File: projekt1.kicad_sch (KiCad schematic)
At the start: 94 parts, among them IC1 TPS563300DRLR, J1 V1, J2 V1, K1 1461103-1, K2 SANYOU_SRD_Form_B, Q1 MMBT3904, Q2 MMBT3904, SW1 SW_Push, SW10 SW_Push, SW11 SW_Push, SW12 SW_Push, SW2 SW_Push, SW3 SW_Push, SW4 SW_Push, SW5 SW_Push, SW6 SW_Push, SW7 SW_Push, SW8 SW_Push, SW9 SW_Push, U1 STM32F030C8Tx, U2 ESP-12E, U4 LTV-824, U5 PN5321A3HN_C1xx, Y1 ABM3-8.000MHZ-D2Y

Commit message: filled all footprints
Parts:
- AE1: value Antena -> Antenna; footprint (none) -> RF_Antenna:Coilcraft_MA5532-AE_RFID
- C1, C10, C11, C12, C13, C14, C15, C16, C17, C18, C19, C2, C20, C21, C22, C23, C24, C25, C26, C27, C28, C29, C3, C30, C31, C32, C4, C5, C6, C7, C8, C9: footprint (none) -> Capacitor_SMD:C_0603_1608Metric_Pad1.08x0.95mm_HandSolder
- J1, J2: footprint (none) -> TerminalBlock_TE-Connectivity:TerminalBlock_TE_282834-2_1x02_P2.54mm_Horizontal
- L1: footprint (none) -> Inductor_SMD:L_0603_1608Metric_Pad1.05x0.95mm_HandSolder
- L2, L3: footprint (none) -> Inductor_SMD:L_0201_0603Metric_Pad0.64x0.40mm_HandSolder
- R1, R10, R11, R12, R13, R14, R15, R17, R18, R19, R2, R4, R6, R7, R8, R9: footprint (none) -> Resistor_SMD:R_0603_1608Metric_Pad0.98x0.95mm_HandSolder
- R16: footprint (none) -> Resistor_SMD:R_0603_1608Metric
- R3: value R -> 300; footprint (none) -> Resistor_SMD:R_0603_1608Metric
- R5: value 10kR -> 10K; footprint (none) -> Resistor_SMD:R_0603_1608Metric_Pad0.98x0.95mm_HandSolder
- SW1, SW10, SW11, SW12, SW2, SW3, SW4, SW5, SW6, SW7, SW8, SW9: footprint (none) -> Button_Switch_SMD:SW_DIP_SPSTx01_Slide_Copal_CHS-01A_W5.08mm_P1.27mm_JPin
- Y1: footprint (none) -> Crystal:Crystal_SMD_Abracon_ABM3-2Pin_5.0x3.2mm_HandSoldering
- Y2: renamed from 27.12MHz1; value CX3225GB -> 27.12MHz1; footprint (none) -> Crystal:Crystal_SMD_Abracon_ABM3-2Pin_5.0x3.2mm_HandSoldering; Memory (none) -> CX3225GB

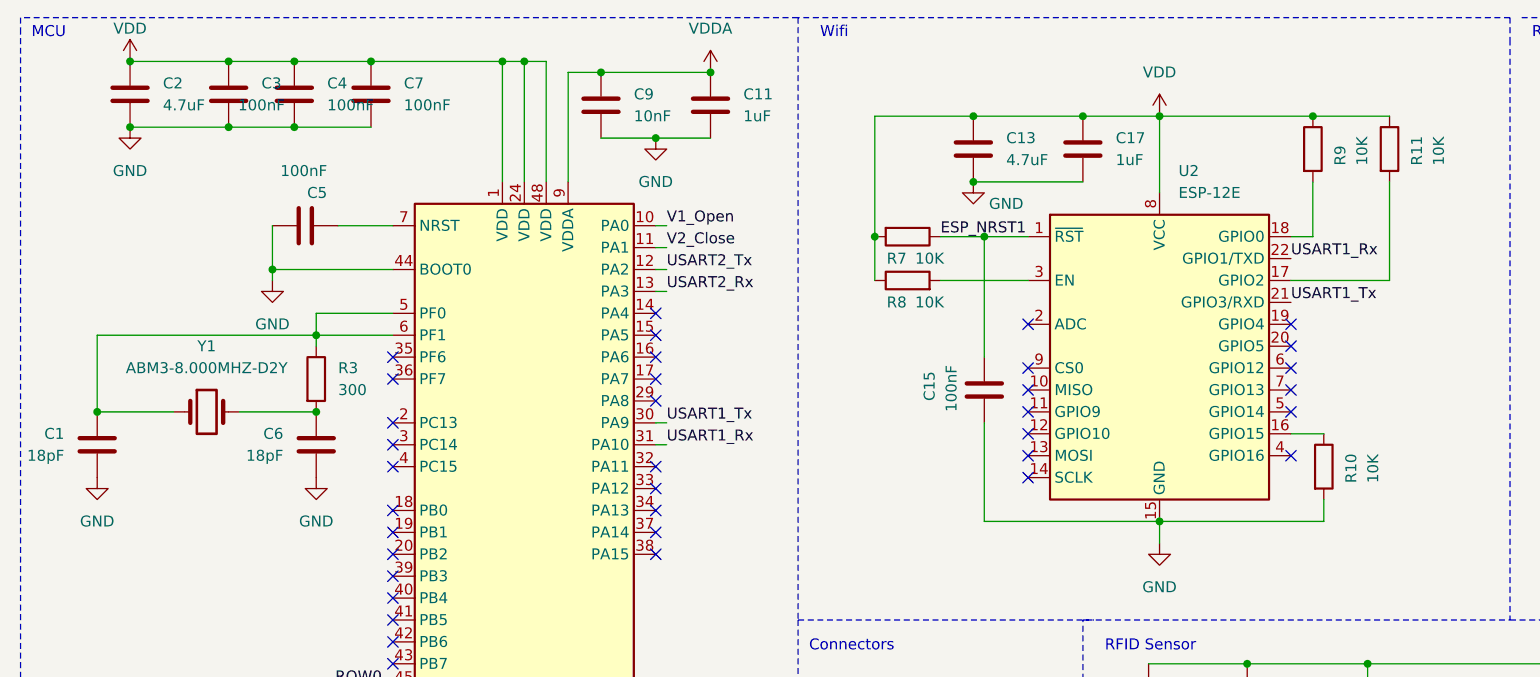
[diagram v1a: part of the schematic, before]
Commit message: initial pcb elements arrangement
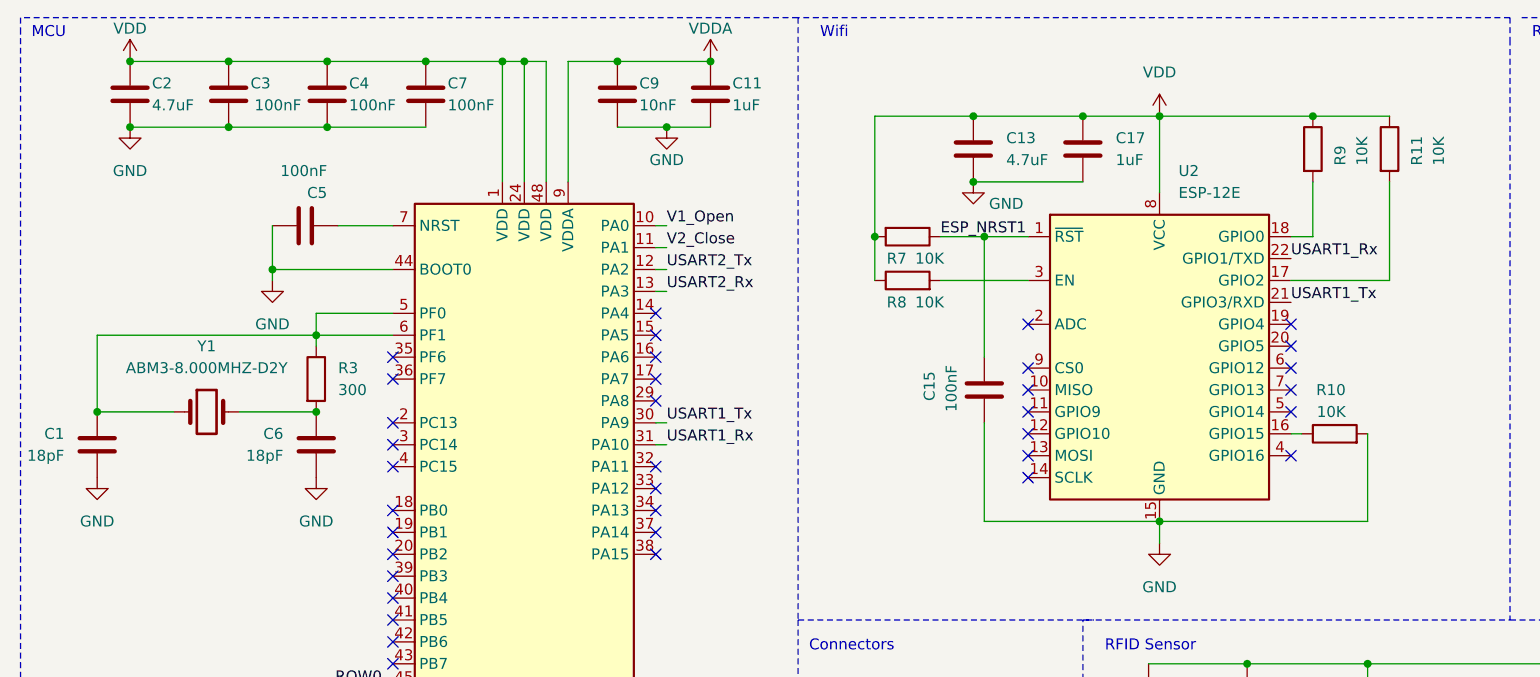
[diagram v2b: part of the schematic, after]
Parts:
- R16: footprint Resistor_SMD:R_0603_1608Metric -> Resistor_SMD:R_0603_1608Metric_Pad0.98x0.95mm_HandSolder
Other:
- moved on the sheet: C11, C4, C7, C9, R10

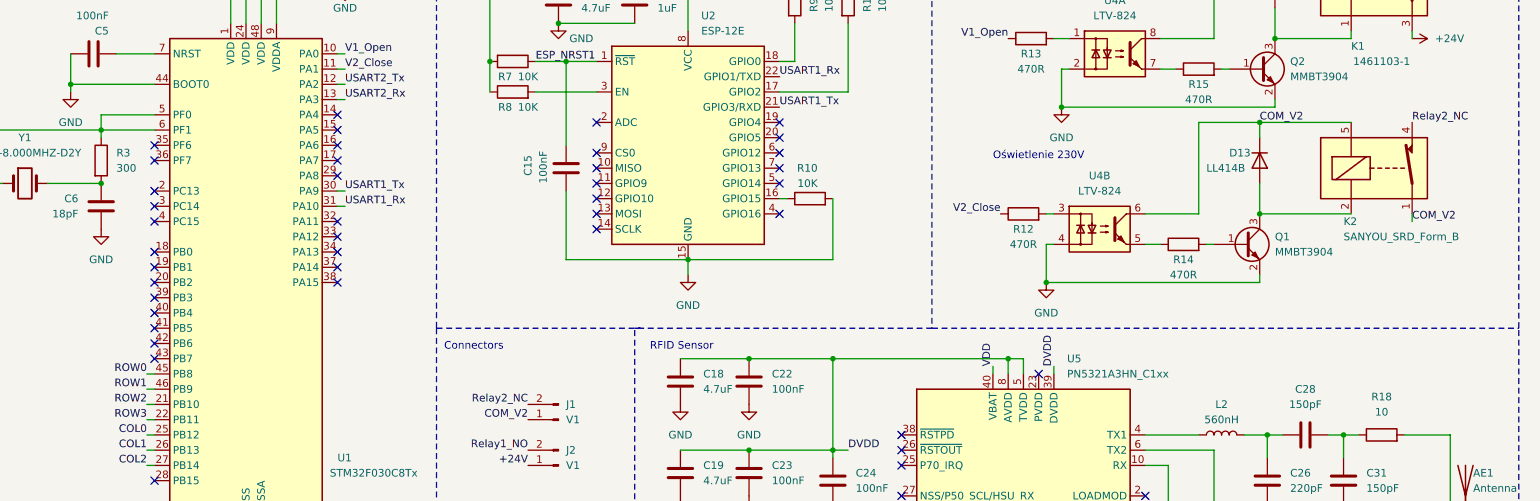
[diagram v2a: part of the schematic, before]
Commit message: pcb connections implemented
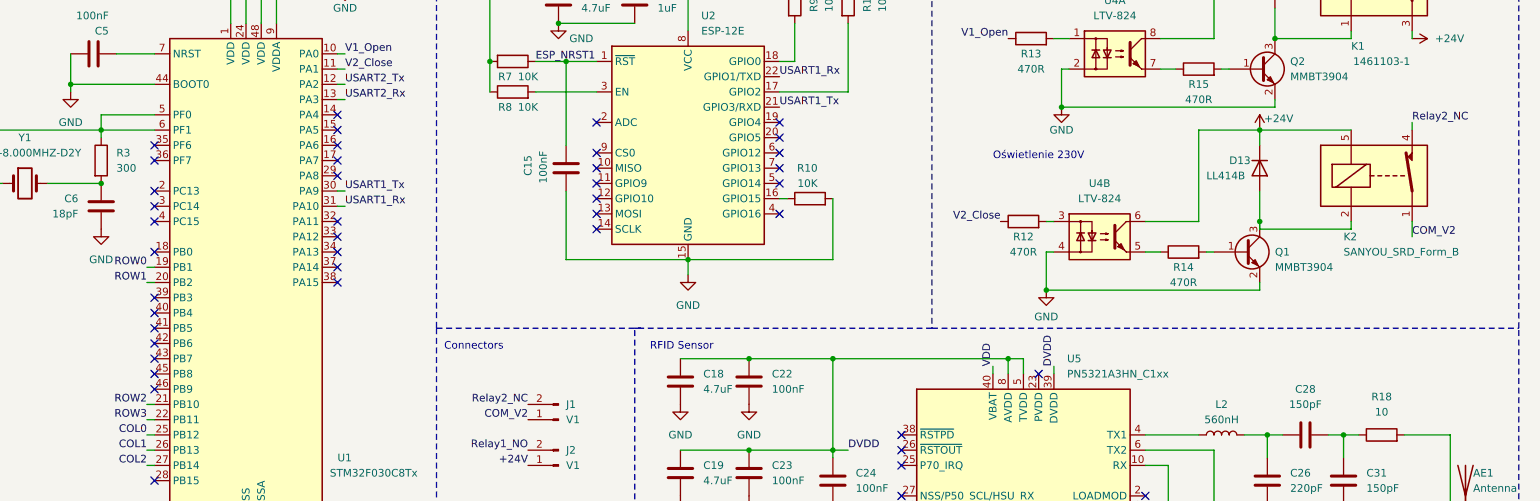
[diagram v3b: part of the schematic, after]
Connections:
- net +24V: now also D13.1 (K), K2.5, U4.6
- net COM_V2: no longer D13.1 (K), K2.5, U4.6
- net ROW0: now also U1.19 (PB1); no longer U1.45 (PB8)
- net ROW1: now also U1.20 (PB2); no longer U1.46 (PB9)
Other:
- moved on the sheet: D13, K2, Q1, R12, R14, U4B

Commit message: changed connector footprint and adjusted paths width
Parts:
- J1: footprint TerminalBlock_TE-Connectivity:TerminalBlock_TE_282834-2_1x02_P2.54mm_Horizontal -> TerminalBlock:TerminalBlock_Altech_AK300-2_P5.00mm
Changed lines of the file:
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@@
       (effects (font (size 1.27 1.27)) (justify right))
     )
-    (property "Footprint" "TerminalBlock_TE-Connectivity:TerminalBlock_TE_282834-2_1x02_P2.54mm_Horizontal" (at 123.19 97.79 0)
+    (property "Footprint" "TerminalBlock:TerminalBlock_Altech_AK300-2_P5.00mm" (at 123.19 97.79 0)
       (effects (font (size 1.27 1.27)) hide)
     )

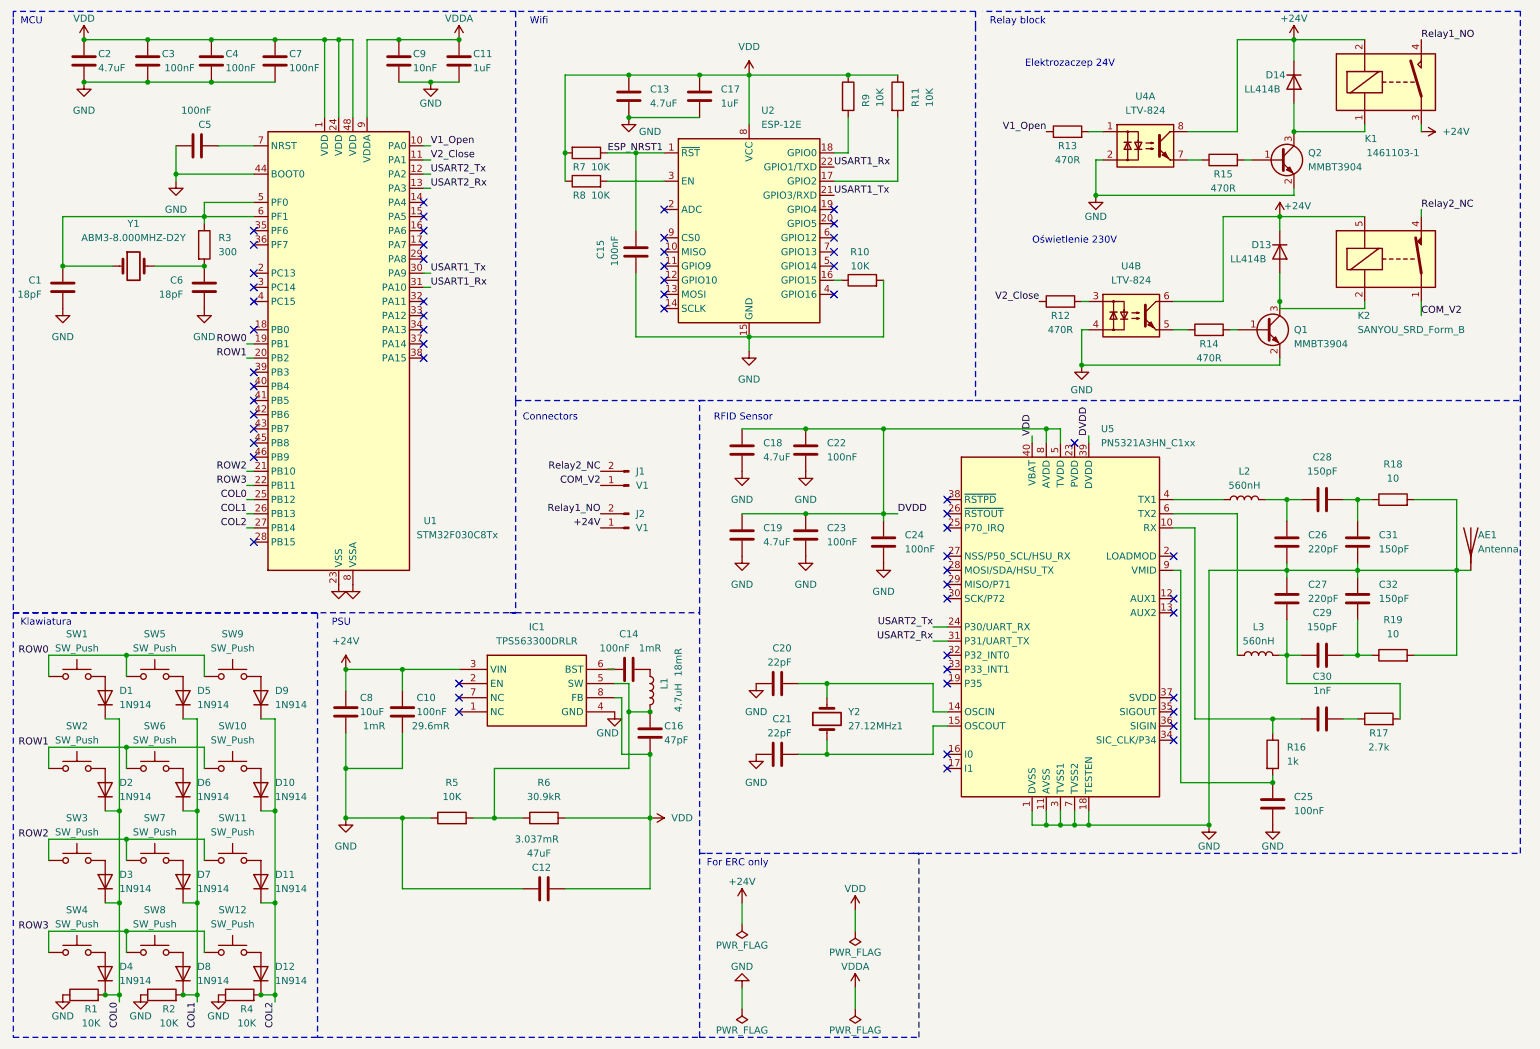
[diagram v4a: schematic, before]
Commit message: add external rfid module connectors
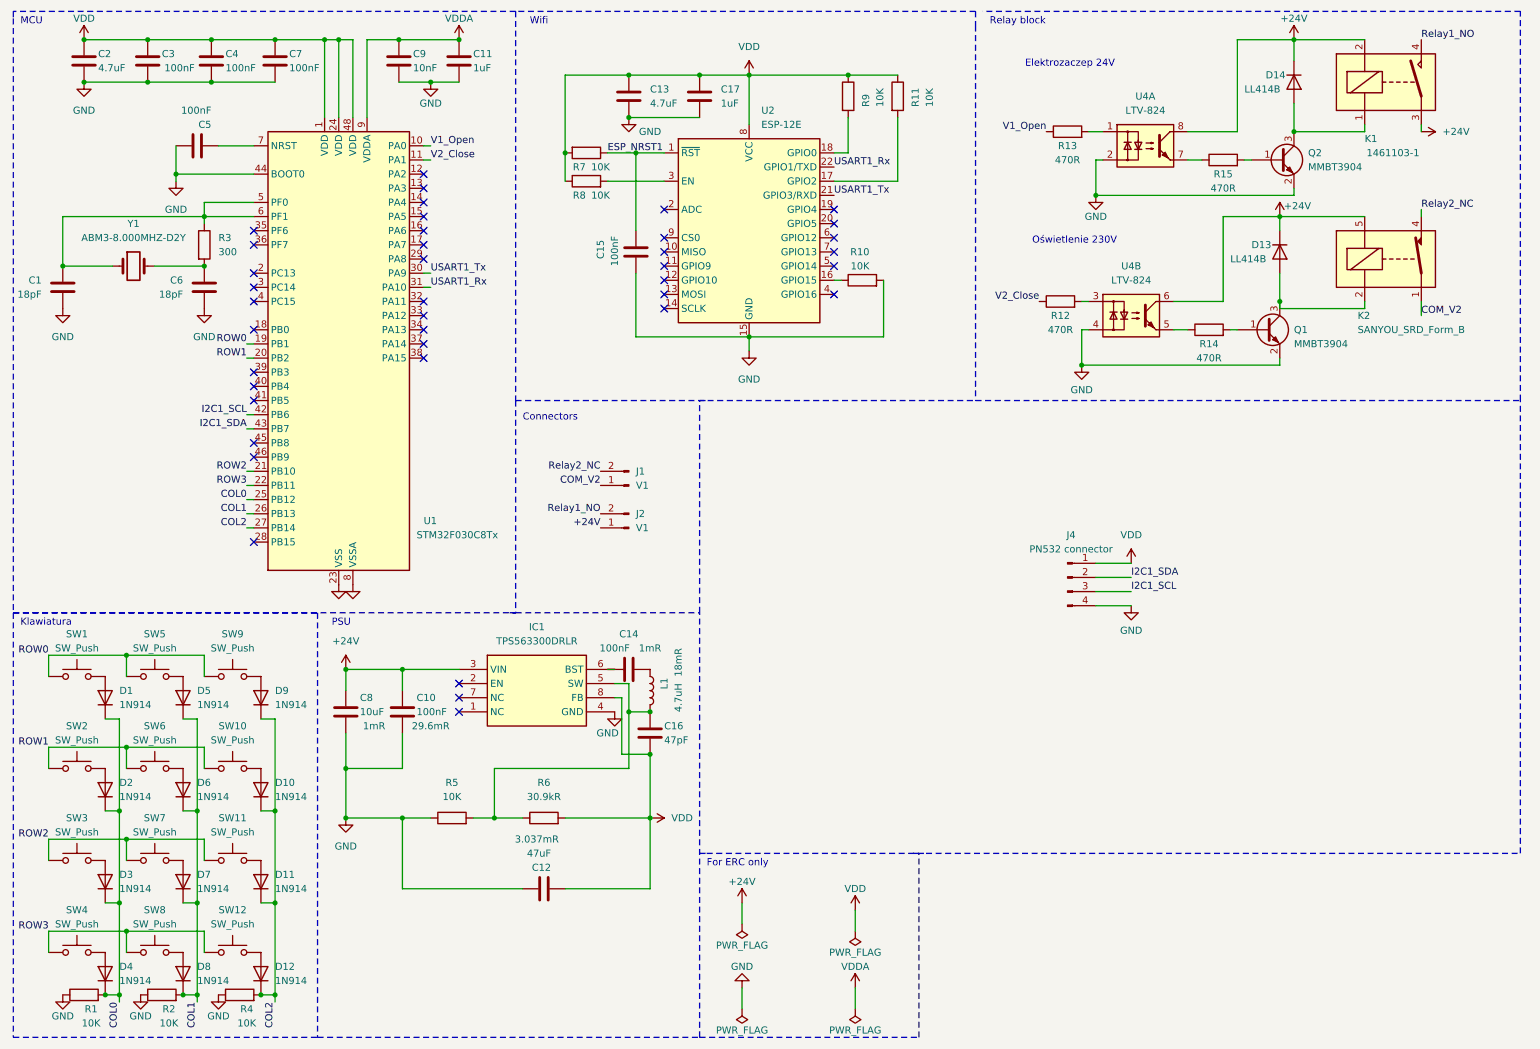
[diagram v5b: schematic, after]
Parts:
- removed AE1: Antenna, RF_Antenna:Coilcraft_MA5532-AE_RFID, symbol Device:Antenna
- removed C18, C19: 4.7uF, Capacitor_SMD:C_0603_1608Metric_Pad1.08x0.95mm_HandSolder, symbol Device:C
- removed C20, C21: 22pF, Capacitor_SMD:C_0603_1608Metric_Pad1.08x0.95mm_HandSolder, symbol Device:C
- removed C22, C23, C24, C25: 100nF, Capacitor_SMD:C_0603_1608Metric_Pad1.08x0.95mm_HandSolder, symbol Device:C
- removed C26, C27: 220pF, Capacitor_SMD:C_0603_1608Metric_Pad1.08x0.95mm_HandSolder, symbol Device:C
- removed C28, C29, C31, C32: 150pF, Capacitor_SMD:C_0603_1608Metric_Pad1.08x0.95mm_HandSolder, symbol Device:C
- removed C30: 1nF, Capacitor_SMD:C_0603_1608Metric_Pad1.08x0.95mm_HandSolder, symbol Device:C
- removed L2, L3: 560nH, Inductor_SMD:L_0201_0603Metric_Pad0.64x0.40mm_HandSolder, symbol Device:L
- removed R16: 1k, Resistor_SMD:R_0603_1608Metric_Pad0.98x0.95mm_HandSolder, symbol Device:R
- removed R17: 2.7k, Resistor_SMD:R_0603_1608Metric_Pad0.98x0.95mm_HandSolder, symbol Device:R
- removed R18, R19: 10, Resistor_SMD:R_0603_1608Metric_Pad0.98x0.95mm_HandSolder, symbol Device:R
- removed U5: PN5321A3HN_C1xx, Package_DFN_QFN:HVQFN-40-1EP_6x6mm_P0.5mm_EP4.1x4.1mm, symbol RF_NFC:PN5321A3HN_C1xx
- removed Y2: 27.12MHz1, Crystal:Crystal_SMD_Abracon_ABM3-2Pin_5.0x3.2mm_HandSoldering, symbol Device:Crystal
- added J4: PN532 connector, Connector_PinHeader_1.00mm:PinHeader_1x04_P1.00mm_Vertical, symbol Connector:Conn_01x04_Pin
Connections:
- net GND: now also J4.4 (Pin_4)
- net VDD: now also J4.1 (Pin_1)
- net I2C1_SCL: now reaches U1.42 (PB6)
- net I2C1_SCL: now also J4.3 (Pin_3)
- net I2C1_SDA: now reaches U1.43 (PB7)
- net I2C1_SDA: now also J4.2 (Pin_2)
- net USART2_Rx: no longer names the net of U1.13 (PA3)
- net USART2_Tx: no longer names the net of U1.12 (PA2)
- no-connect marks 60 -> 40
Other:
- note removed: "RFID Sensor"
- company: (none) -> Kacper Nowaczyk Robert Dobrowolski
- title: (none) -> Prototyp układu kontroli dostępu
